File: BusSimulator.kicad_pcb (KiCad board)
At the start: 2 copper layers, 101.6 x 53.4 mm, 100 parts, among them IC1 CS30CL, IC2 CS30CL, IC3 CS30CL, J1 CONN_3-6318491-6, J2 OSTTA024163, J3 Conn_01x03, J4 Conn_01x03, J5 Conn_01x02, J6 Conn_01x03, Q1 MOSFET_N, Q2 MOSFET_N, Q3 MOSFET_N, U1 MPM3620, U2 MPM3620, U3 MCP6H04-E/SL, U4 ADC128D818CIMTX, U5 ISO1540DR, U6 Si8660_SOIC-16, U7 Si8660_SOIC-16, U8 Si8660_SOIC-16, U9 MSATA-Socket

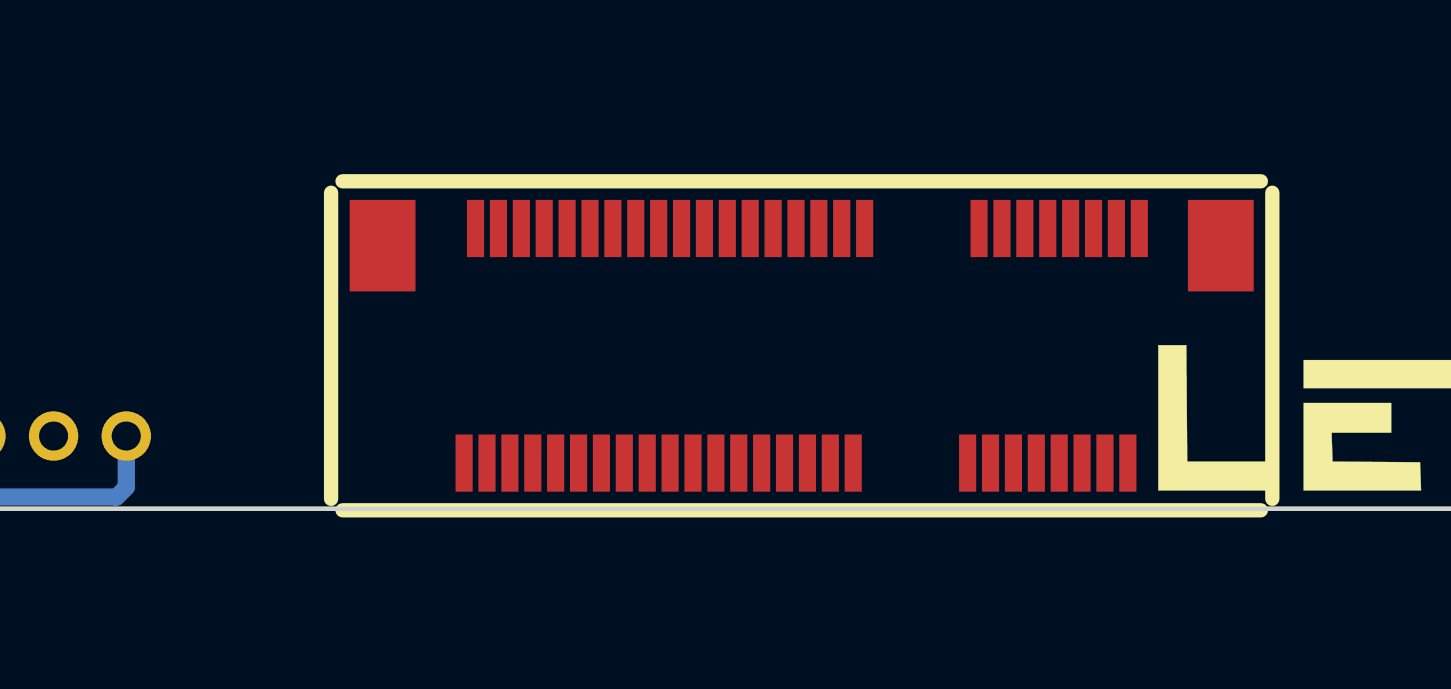
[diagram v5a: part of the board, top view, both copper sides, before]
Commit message: Fix mosfets
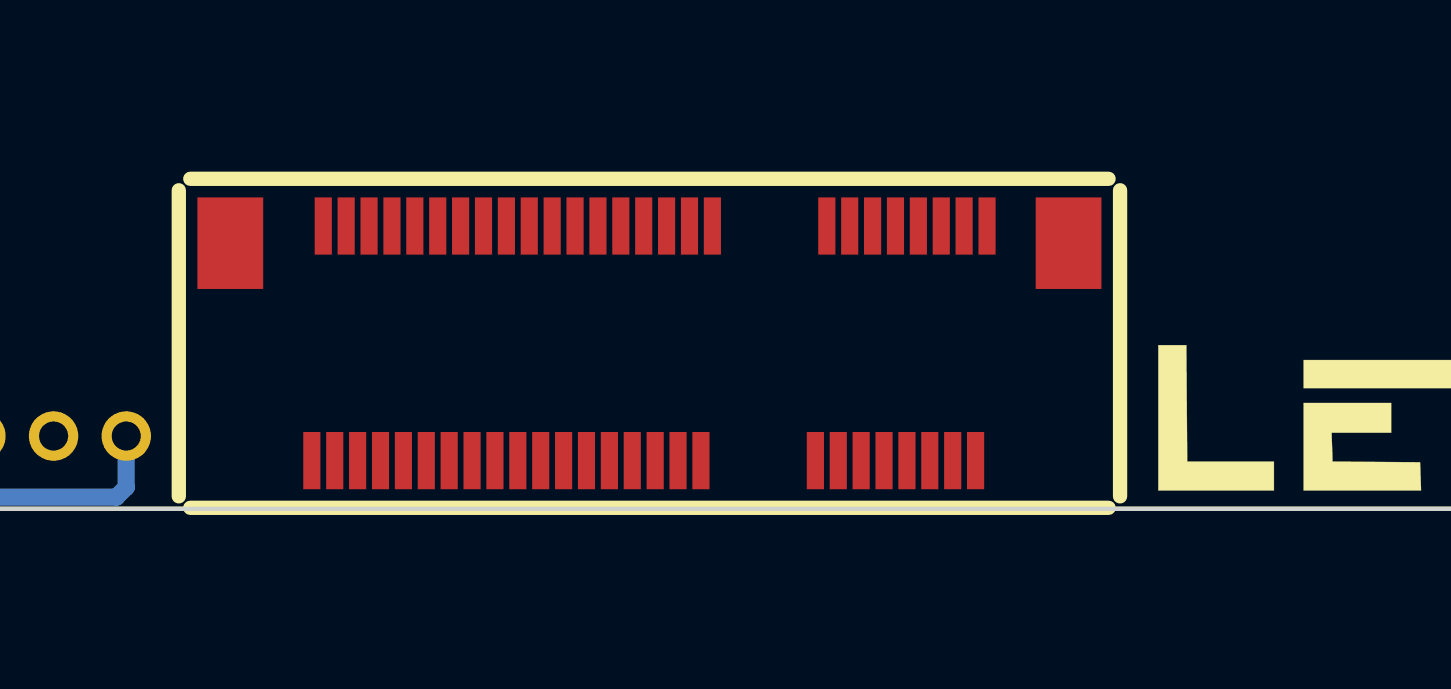
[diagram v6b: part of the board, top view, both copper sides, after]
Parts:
- moved U9 5.32 mm to (176.5, 136.1)
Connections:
- C25 pad 1: FC5V -> (no net)
- C29 pad 1: Net-(C29-Pad1) -> (no net)
- C30 pad 1: Net-(C30-Pad1) -> (no net)
- C31 pad 1: Net-(C31-Pad1) -> (no net)
- J1 pad 10: Net-(J1-Pad10) -> (no net)
- J1 pad 101: Net-(J1-Pad101) -> (no net)
- J1 pad 102: Net-(J1-Pad102) -> (no net)
- J1 pad 103: Net-(J1-Pad103) -> (no net)
- J1 pad 112: Net-(J1-Pad112) -> (no net)
- J1 pad 113: Net-(J1-Pad113) -> (no net)
- J1 pad 114: Net-(J1-Pad114) -> (no net)
- J1 pad 115: Net-(J1-Pad115) -> (no net)
- J1 pad 116: Net-(J1-Pad116) -> (no net)
- J1 pad 117: Net-(J1-Pad117) -> (no net)
- J1 pad 118: Net-(J1-Pad118) -> (no net)
- J1 pad 119: Net-(J1-Pad119) -> (no net)
- J1 pad 12: Net-(J1-Pad12) -> (no net)
- J1 pad 120: Net-(J1-Pad120) -> (no net)
- J1 pad 123: Net-(J1-Pad123) -> (no net)
- J1 pad 124: Net-(J1-Pad124) -> (no net)
- J1 pad 125: Net-(J1-Pad125) -> (no net)
- J1 pad 126: Net-(J1-Pad126) -> (no net)
- J1 pad 127: Net-(J1-Pad127) -> (no net)
- J1 pad 128: Net-(J1-Pad128) -> (no net)
- J1 pad 129: Net-(J1-Pad129) -> (no net)
- J1 pad 13: Net-(J1-Pad13) -> (no net)
- J1 pad 130: Net-(J1-Pad130) -> (no net)
- J1 pad 132: Net-(J1-Pad132) -> (no net)
- J1 pad 133: Net-(J1-Pad133) -> (no net)
- J1 pad 135: Net-(J1-Pad135) -> (no net)
- J1 pad 136: Net-(J1-Pad136) -> (no net)
- J1 pad 137: Net-(J1-Pad137) -> (no net)
- J1 pad 138: Net-(J1-Pad138) -> (no net)
- J1 pad 139: Net-(J1-Pad139) -> (no net)
- J1 pad 14: Net-(J1-Pad14) -> (no net)
- J1 pad 140: Net-(J1-Pad140) -> (no net)
- J1 pad 142: Net-(J1-Pad142) -> (no net)
- J1 pad 145: Net-(J1-Pad145) -> (no net)
- J1 pad 146: Net-(J1-Pad146) -> (no net)
- J1 pad 147: Net-(J1-Pad147) -> (no net)
- J1 pad 148: Net-(J1-Pad148) -> (no net)
- J1 pad 149: Net-(J1-Pad149) -> (no net)
- J1 pad 15: Net-(J1-Pad15) -> (no net)
- J1 pad 150: Net-(J1-Pad150) -> (no net)
- J1 pad 152: Net-(J1-Pad152) -> (no net)
- J1 pad 153: Net-(J1-Pad153) -> (no net)
- J1 pad 154: Net-(J1-Pad154) -> (no net)
- J1 pad 155: Net-(J1-Pad155) -> (no net)
- J1 pad 156: Net-(J1-Pad156) -> (no net)
- J1 pad 157: Net-(J1-Pad157) -> (no net)
- J1 pad 158: Net-(J1-Pad158) -> (no net)
- J1 pad 160: Net-(J1-Pad160) -> (no net)
- J1 pad 162: Net-(J1-Pad162) -> (no net)
- J1 pad 163: Net-(J1-Pad163) -> (no net)
- J1 pad 165: Net-(J1-Pad165) -> (no net)
- J1 pad 166: Net-(J1-Pad166) -> (no net)
- J1 pad 168: Net-(J1-Pad168) -> (no net)
- J1 pad 169: Net-(J1-Pad169) -> (no net)
- J1 pad 171: Net-(J1-Pad171) -> (no net)
- J1 pad 172: Net-(J1-Pad172) -> (no net)
- J1 pad 174: Net-(J1-Pad174) -> (no net)
- J1 pad 175: Net-(J1-Pad175) -> (no net)
- J1 pad 176: Net-(J1-Pad176) -> (no net)
- J1 pad 178: Net-(J1-Pad178) -> (no net)
- J1 pad 179: Net-(J1-Pad179) -> (no net)
- J1 pad 18: Net-(J1-Pad18) -> (no net)
- J1 pad 181: Net-(J1-Pad181) -> (no net)
- J1 pad 182: Net-(J1-Pad182) -> (no net)
- J1 pad 183: Net-(J1-Pad183) -> (no net)
- J1 pad 184: Net-(J1-Pad184) -> (no net)
- J1 pad 185: Net-(J1-Pad185) -> (no net)
- J1 pad 186: Net-(J1-Pad186) -> (no net)
- J1 pad 187: Net-(J1-Pad187) -> (no net)
- J1 pad 188: Net-(J1-Pad188) -> (no net)
- J1 pad 189: Net-(J1-Pad189) -> (no net)
- J1 pad 191: Net-(J1-Pad191) -> (no net)
- J1 pad 192: Net-(J1-Pad192) -> (no net)
- J1 pad 193: Net-(J1-Pad193) -> (no net)
- J1 pad 198: Net-(J1-Pad198) -> (no net)
- J1 pad 199: Net-(J1-Pad199) -> (no net)
- J1 pad 2: Net-(J1-Pad2) -> (no net)
- J1 pad 201: Net-(J1-Pad201) -> (no net)
- J1 pad 202: Net-(J1-Pad202) -> (no net)
- J1 pad 203: Net-(J1-Pad203) -> (no net)
- J1 pad 204: Net-(J1-Pad204) -> (no net)
- J1 pad 205: Net-(J1-Pad205) -> (no net)
- J1 pad 206: Net-(J1-Pad206) -> (no net)
- J1 pad 207: Net-(J1-Pad207) -> (no net)
- J1 pad 208: Net-(J1-Pad208) -> (no net)
- J1 pad 209: Net-(J1-Pad209) -> (no net)
- J1 pad 211: Net-(J1-Pad211) -> (no net)
- J1 pad 212: Net-(J1-Pad212) -> (no net)
- J1 pad 22: Net-(J1-Pad22) -> (no net)
- J1 pad 23: Net-(J1-Pad23) -> (no net)
- J1 pad 24: Net-(J1-Pad24) -> (no net)
- J1 pad 25: Net-(J1-Pad25) -> (no net)
- J1 pad 26: Net-(J1-Pad26) -> (no net)
- J1 pad 27: Net-(J1-Pad27) -> (no net)
- J1 pad 29: Net-(J1-Pad29) -> (no net)
- J1 pad 3: Net-(J1-Pad3) -> (no net)
- J1 pad 30: Net-(J1-Pad30) -> (no net)
- J1 pad 32: Net-(J1-Pad32) -> (no net)
- J1 pad 33: Net-(J1-Pad33) -> (no net)
- J1 pad 34: Net-(J1-Pad34) -> (no net)
- J1 pad 35: Net-(J1-Pad35) -> (no net)
- J1 pad 36: Net-(J1-Pad36) -> (no net)
- J1 pad 37: Net-(J1-Pad37) -> (no net)
- J1 pad 38: Net-(J1-Pad38) -> (no net)
- J1 pad 39: Net-(J1-Pad39) -> (no net)
- J1 pad 4: Net-(J1-Pad4) -> (no net)
- J1 pad 40: Net-(J1-Pad40) -> (no net)
- J1 pad 42: Net-(J1-Pad42) -> (no net)
- J1 pad 43: Net-(J1-Pad43) -> (no net)
- J1 pad 44: Net-(J1-Pad44) -> (no net)
- J1 pad 45: Net-(J1-Pad45) -> (no net)
- J1 pad 46: Net-(J1-Pad46) -> (no net)
- J1 pad 47: Net-(J1-Pad47) -> (no net)
- J1 pad 48: Net-(J1-Pad48) -> (no net)
- J1 pad 49: Net-(J1-Pad49) -> (no net)
- J1 pad 5: Net-(J1-Pad5) -> (no net)
- J1 pad 50: Net-(J1-Pad50) -> (no net)
- J1 pad 52: Net-(J1-Pad52) -> (no net)
- J1 pad 53: Net-(J1-Pad53) -> (no net)
- J1 pad 55: Net-(J1-Pad55) -> (no net)
- J1 pad 56: Net-(J1-Pad56) -> (no net)
- J1 pad 58: Net-(J1-Pad58) -> (no net)
- J1 pad 59: Net-(J1-Pad59) -> (no net)
- J1 pad 6: Net-(J1-Pad6) -> (no net)
- J1 pad 61: Net-(J1-Pad61) -> (no net)
- J1 pad 62: Net-(J1-Pad62) -> (no net)
- J1 pad 64: Net-(J1-Pad64) -> (no net)
- J1 pad 65: Net-(J1-Pad65) -> (no net)
- J1 pad 68: Net-(J1-Pad68) -> (no net)
- J1 pad 69: Net-(J1-Pad69) -> (no net)
- J1 pad 7: Net-(J1-Pad7) -> (no net)
- J1 pad 71: Net-(J1-Pad71) -> (no net)
- J1 pad 72: Net-(J1-Pad72) -> (no net)
- J1 pad 73: Net-(J1-Pad73) -> (no net)
- J1 pad 74: Net-(J1-Pad74) -> (no net)
- J1 pad 75: Net-(J1-Pad75) -> (no net)
- J1 pad 76: Net-(J1-Pad76) -> (no net)
- J1 pad 77: Net-(J1-Pad77) -> (no net)
- J1 pad 78: Net-(J1-Pad78) -> (no net)
- J1 pad 79: Net-(J1-Pad79) -> (no net)
- J1 pad 8: Net-(J1-Pad8) -> (no net)
- J1 pad 81: Net-(J1-Pad81) -> (no net)
- J1 pad 82: Net-(J1-Pad82) -> (no net)
- J1 pad 83: Net-(J1-Pad83) -> (no net)
- J1 pad 84: Net-(J1-Pad84) -> (no net)
- J1 pad 86: Net-(J1-Pad86) -> (no net)
- J1 pad 87: Net-(J1-Pad87) -> (no net)
- J1 pad 88: Net-(J1-Pad88) -> (no net)
- J1 pad 89: Net-(J1-Pad89) -> (no net)
- J1 pad 9: Net-(J1-Pad9) -> (no net)
- J1 pad 91: Net-(J1-Pad91) -> (no net)
- J1 pad 92: Net-(J1-Pad92) -> (no net)
- J1 pad 94: Net-(J1-Pad94) -> (no net)
- J1 pad 95: Net-(J1-Pad95) -> (no net)
- J1 pad 96: Net-(J1-Pad96) -> (no net)
- J1 pad 97: Net-(J1-Pad97) -> (no net)
- SHIELD1 pad 14: Net-(SHIELD1-Pad14) -> (no net)
- SHIELD1 pad 15: Net-(SHIELD1-Pad15) -> (no net)
- SHIELD1 pad 16: Net-(SHIELD1-Pad16) -> (no net)
- SHIELD1 pad 17: Net-(SHIELD1-Pad17) -> (no net)
- SHIELD1 pad 18: Net-(SHIELD1-Pad18) -> (no net)
- SHIELD1 pad 19: Net-(SHIELD1-Pad19) -> (no net)
- SHIELD1 pad 20: Net-(SHIELD1-Pad20) -> (no net)
- SHIELD1 pad 21: Net-(SHIELD1-Pad21) -> (no net)
- SHIELD1 pad 26: Net-(SHIELD1-Pad26) -> (no net)
- SHIELD1 pad 27: Net-(SHIELD1-Pad27) -> (no net)
- SHIELD1 pad 28: Net-(SHIELD1-Pad28) -> (no net)
- SHIELD1 pad 29: Net-(SHIELD1-Pad29) -> (no net)
- SHIELD1 pad 30: Net-(SHIELD1-Pad30) -> (no net)
- SHIELD1 pad 31: Net-(SHIELD1-Pad31) -> (no net)
- SHIELD1 pad 38: Net-(SHIELD1-Pad38) -> (no net)
- SHIELD1 pad 39: Net-(SHIELD1-Pad39) -> (no net)
- SHIELD1 pad 40: Net-(SHIELD1-Pad40) -> (no net)
- SHIELD1 pad 41: Net-(SHIELD1-Pad41) -> (no net)
- SHIELD1 pad 42: Net-(SHIELD1-Pad42) -> (no net)
- SHIELD1 pad 43: Net-(SHIELD1-Pad43) -> (no net)
- SHIELD1 pad IO_R: Net-(SHIELD1-PadIO_R) -> (no net)
- SHIELD1 pad RST: Net-(SHIELD1-PadRST) -> (no net)
- U1 pad 11: Net-(U1-Pad11) -> (no net)
- U1 pad 2: Net-(U1-Pad2) -> (no net)
- U1 pad 4: Net-(U1-Pad4) -> (no net)
- U1 pad 5: Net-(U1-Pad5) -> (no net)
- U1 pad 6: Net-(U1-Pad6) -> (no net)
- U2 pad 11: Net-(U2-Pad11) -> (no net)
- U2 pad 2: Net-(U2-Pad2) -> (no net)
- U2 pad 4: Net-(U2-Pad4) -> (no net)
- U2 pad 5: Net-(U2-Pad5) -> (no net)
- U2 pad 6: Net-(U2-Pad6) -> (no net)
- U4 pad 6: Net-(U4-Pad6) -> (no net)
- U4 pad 9: Net-(U4-Pad9) -> (no net)
- U9 pad 1: Net-(U9-Pad1) -> (no net)
- U9 pad 10: Net-(U9-Pad10) -> (no net)
- U9 pad 11: Net-(U9-Pad11) -> (no net)
- U9 pad 12: Net-(U9-Pad12) -> (no net)
- U9 pad 13: Net-(U9-Pad13) -> (no net)
- U9 pad 14: Net-(U9-Pad14) -> (no net)
- U9 pad 16: Net-(U9-Pad16) -> (no net)
- U9 pad 17: Net-(U9-Pad17) -> (no net)
- U9 pad 19: Net-(U9-Pad19) -> (no net)
- U9 pad 20: Net-(U9-Pad20) -> (no net)
- U9 pad 22: Net-(U9-Pad22) -> (no net)
- U9 pad 28: Net-(U9-Pad28) -> (no net)
- U9 pad 3: Net-(U9-Pad3) -> (no net)
- U9 pad 30: Net-(U9-Pad30) -> (no net)
- U9 pad 32: Net-(U9-Pad32) -> (no net)
- U9 pad 36: Net-(U9-Pad36) -> (no net)
- U9 pad 38: Net-(U9-Pad38) -> (no net)
- U9 pad 42: Net-(U9-Pad42) -> (no net)
- U9 pad 43: Net-(U9-Pad43) -> (no net)
- U9 pad 44: Net-(U9-Pad44) -> (no net)
- U9 pad 45: Net-(U9-Pad45) -> (no net)
- U9 pad 46: Net-(U9-Pad46) -> (no net)
- U9 pad 47: Net-(U9-Pad47) -> (no net)
- U9 pad 48: Net-(U9-Pad48) -> (no net)
- U9 pad 5: Net-(U9-Pad5) -> (no net)
- U9 pad 6: Net-(U9-Pad6) -> (no net)
- U9 pad 7: Net-(U9-Pad7) -> (no net)
- U9 pad 8: Net-(U9-Pad8) -> (no net)

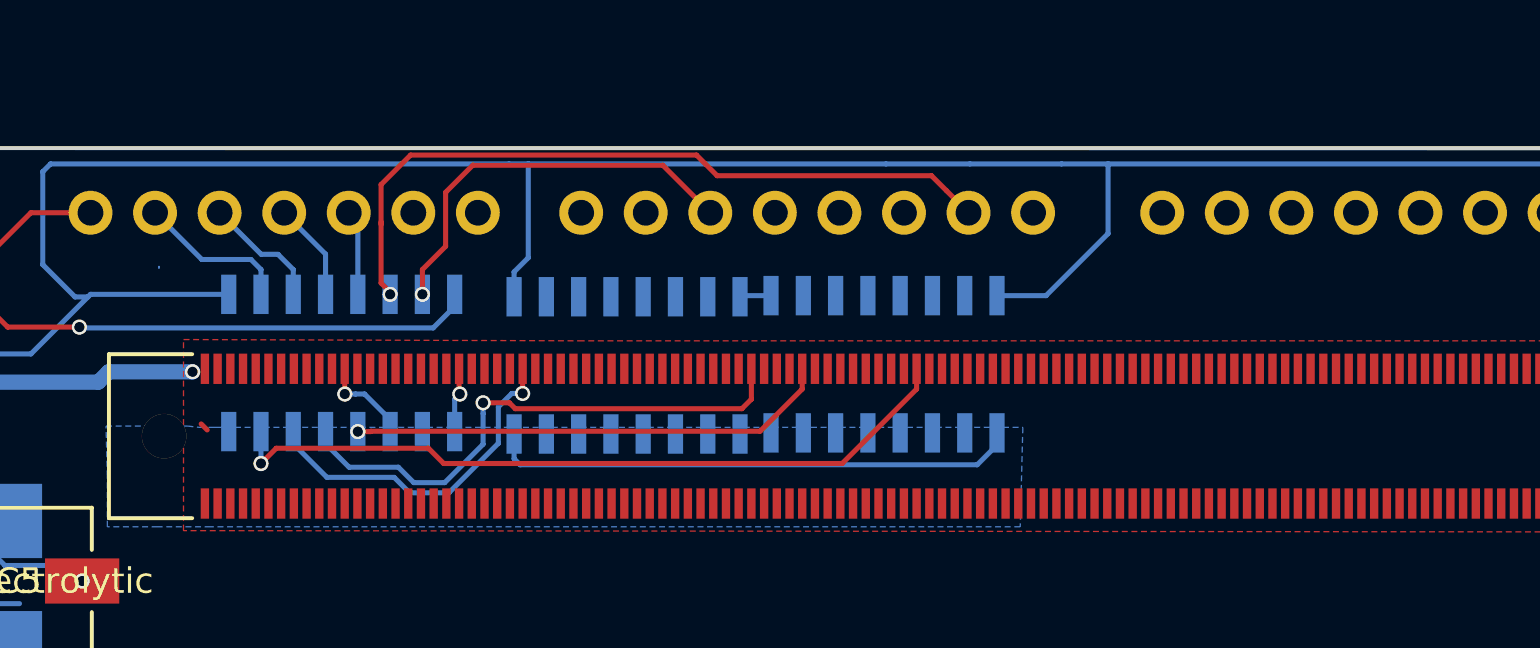
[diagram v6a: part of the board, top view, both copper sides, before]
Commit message: Organize isolator nets and arrange PCB components
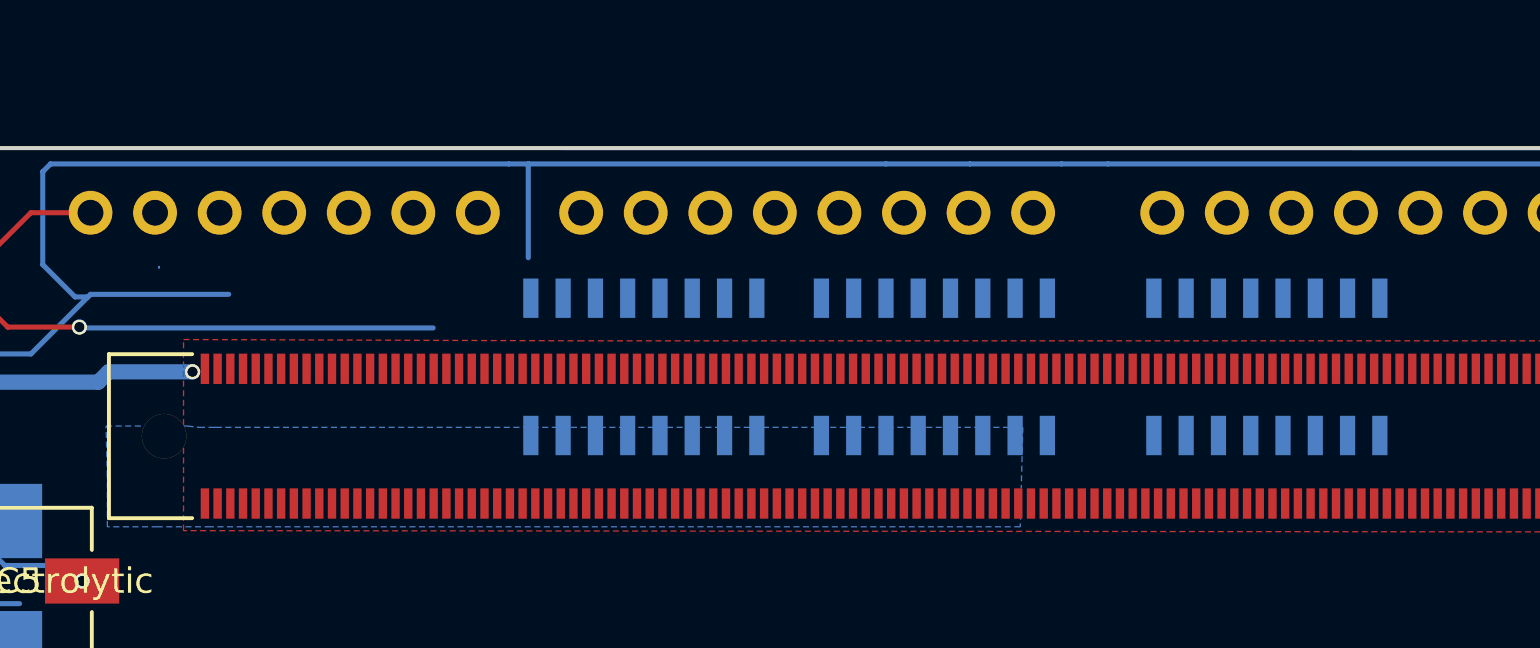
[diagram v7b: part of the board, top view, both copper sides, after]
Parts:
- U6: value Si8660_SOIC-16 -> ISOInputs_Si8660_SOIC-16
- U7, U8: value Si8660_SOIC-16 -> ISOOutputs_Si8660_SOIC-16
- moved U8 25.2 mm to (182.9, 97.2)
- moved U7 11.9 mm to (158.4, 97.2)
- moved U6 1.98 mm to (169.8, 97.2)
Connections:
- C12 pad 2: GND -> mCOM_GND
- C14 pad 2: GND -> mCOM_GND
- C8 pad 2: mCOM_GND -> GND
- C9 pad 1: mCOM_GND -> GND
- J1 pad 98: SER0_TX -> mCOM_TX
- J1 pad 99: SER0_RX -> mCOM_RX
- Q1 pad G: ISO_LOAD_1 -> LOAD_1
- Q2 pad G: ISO_LOAD_2 -> LOAD_2
- Q3 pad G: ISO_LOAD_3 -> LOAD_3
- U6 pad 10: ISO_GPO3 -> ISOSERO_Rx
- U6 pad 11: ISO_GPO2 -> ISO_GPO0
- U6 pad 12: ISO_GPO1 -> ISO_GPO3
- U6 pad 13: ISO_GPO0 -> ISO_GPO2
- U6 pad 14: ISOSERO_Tx -> ISO_GPO1
- U6 pad 3: SER0_TX -> GPO1
- U6 pad 4: GPO0 -> GPO2
- U6 pad 5: GPO1 -> GPO3
- U6 pad 6: GPO2 -> GPO0
- U6 pad 7: GPO3 -> mCOM_TX
- U7 pad 10: LOAD_1 -> WAKE1n
- U7 pad 11: SER0_RX -> GPI1
- U7 pad 12: GPI1 -> GPI2
- U7 pad 13: GPI2 -> GPI3
- U7 pad 14: GPI3 -> mCOM_RX
- U7 pad 15: GPI0 -> SLEEPn
- U7 pad 2: ISO_GPI0 -> ISO_SLEEPn
- U7 pad 3: ISO_GPI1 -> ISOSERO_Tx
- U7 pad 4: ISO_GPI2 -> ISO_GPI3
- U7 pad 5: ISO_GPI3 -> ISO_GPI2
- U7 pad 6: ISOSERO_Rx -> ISO_GPI1
- U7 pad 7: ISO_LOAD_1 -> ISOWAKE1n
- U8 pad 10: ISO_LOAD_3 -> PWRBTNn
- U8 pad 11: ISO_LOAD_2 -> LOAD_3
- U8 pad 12: WAKE1n -> LOAD_2
- U8 pad 13: SLEEPn -> LOAD_1
- U8 pad 14: SYS_RESETn -> GPI0
- U8 pad 15: PWRBTNn -> SYS_RESETn
- U8 pad 2: ISOPWRBTNn -> ISOSYS_RESETn
- U8 pad 3: ISOSYS_RESETn -> ISO_GPI0
- U8 pad 4: ISO_SLEEPn -> ISO_LOAD_1
- U8 pad 5: ISOWAKE1n -> ISO_LOAD_2
- U8 pad 6: LOAD_2 -> ISO_LOAD_3
- U8 pad 7: LOAD_3 -> ISOPWRBTNn
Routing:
- net GPI0: track 29.6 -> 0.00 mm, vias 1 -> 0
- net ISOSERO_Rx: track 29.1 -> 0.00 mm, vias 1 -> 0
- net GPI2: track 21.6 -> 0.00 mm, vias 1 -> 0
- net +3.3V: track 50.6 -> 29.7 mm
- net GPI1: track 19.0 -> 0.00 mm, vias 1 -> 0
- net ISO_LOAD_1: track 16.0 -> 0.00 mm, vias 1 -> 0
- net GPI3: track 13.9 -> 0.00 mm, vias 1 -> 0
- net FC3V3: track 191.9 -> 182.0 mm
- net ISO_GPI0: track 6.07 -> 0.00 mm
- net ISO_GPI1: track 4.80 -> 0.00 mm
- net ISO_GPI2: track 3.88 -> 0.00 mm
- net SER0_RX: track 3.67 -> 0.00 mm, vias 1 -> 0
- net GND: track 28.5 -> 25.6 mm
- net ISO_GPI3: track 3.36 -> 0.51 mm
- net mCOM_GND: track 131.6 -> 129.0 mm, vias 5 -> 4
